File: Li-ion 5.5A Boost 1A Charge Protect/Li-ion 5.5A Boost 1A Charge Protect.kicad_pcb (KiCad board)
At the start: 2 copper layers, 51.5 x 32 mm, 58 parts, among them J1 USB_C_FEMALE, Q1 BUK6D30-40E, SW1 SW_DPST, U1 AP9101CK6, U2 ECH8695R-TL-W, U3 MCP73833T, U4 PAM2423AECADJR

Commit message: Fixed position on diode.
Fixed position on diode.
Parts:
- moved D1 1.20 mm to (133.0, 86.0)

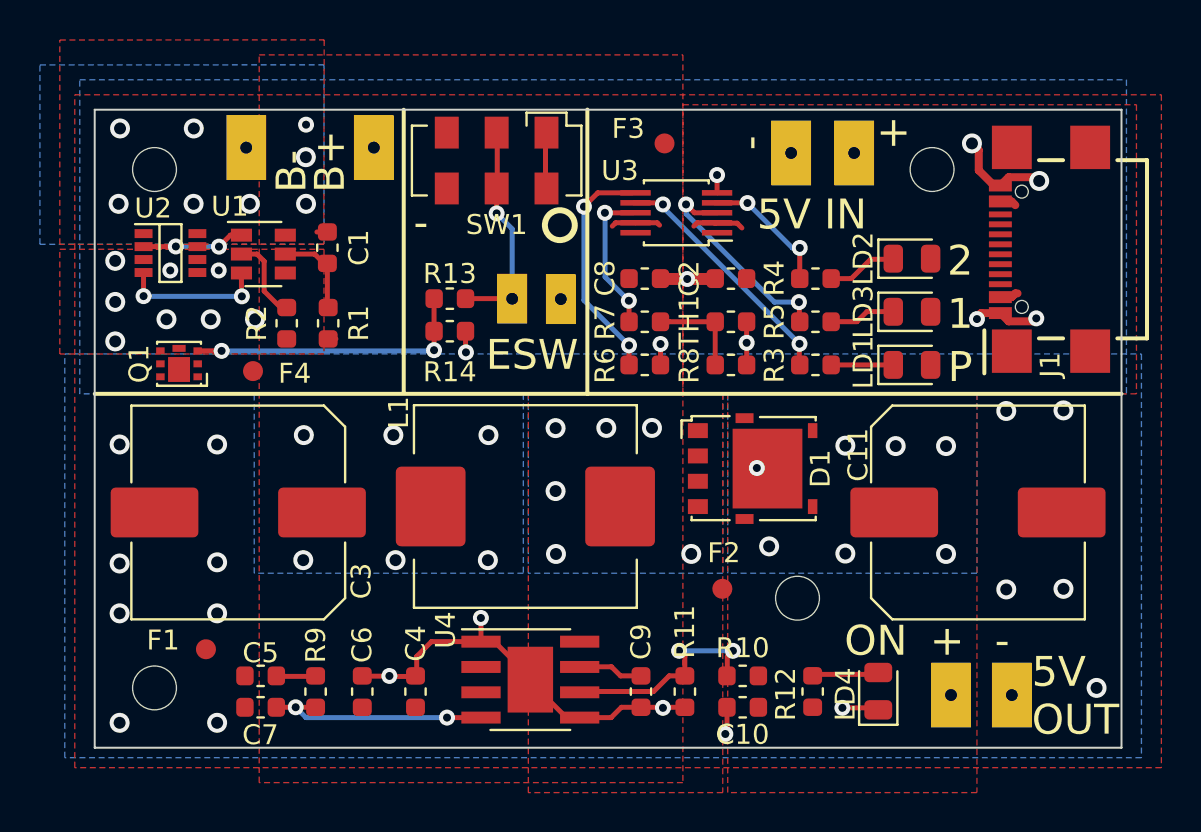
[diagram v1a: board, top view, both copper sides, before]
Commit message: Updates for footprint corrections.
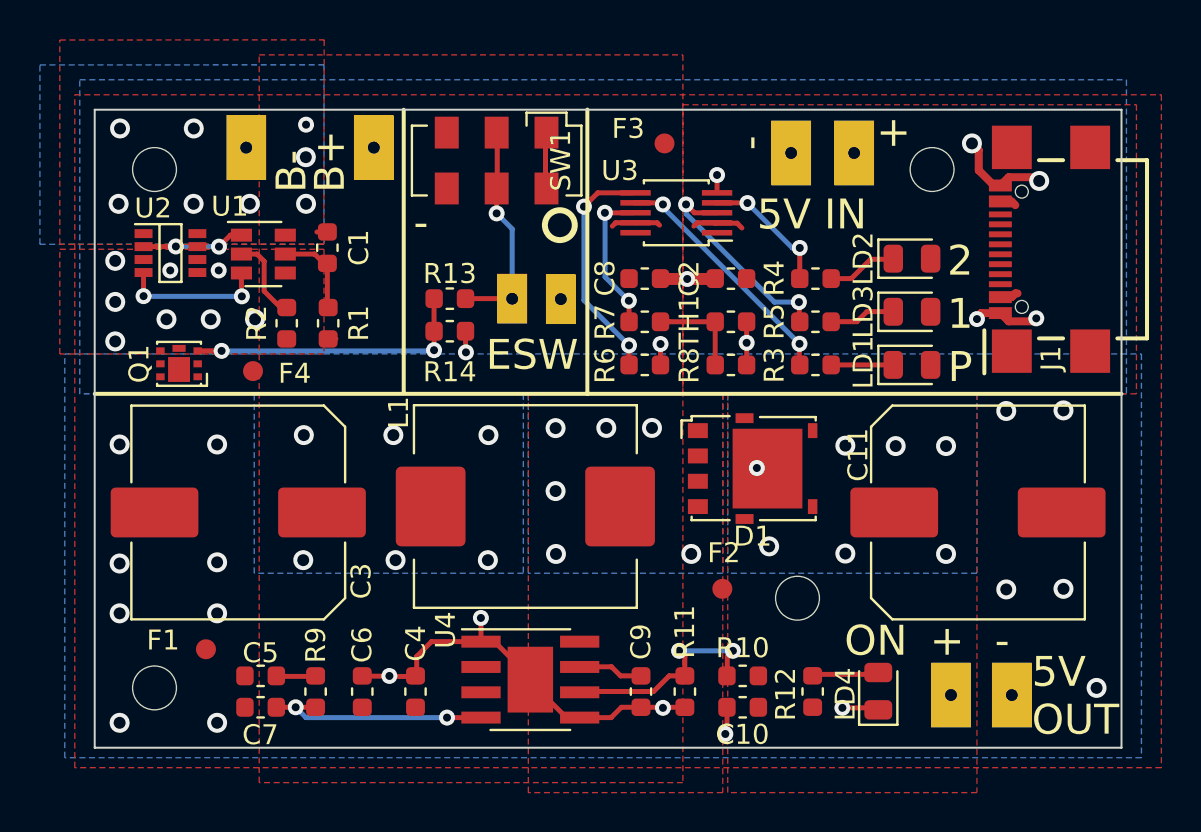
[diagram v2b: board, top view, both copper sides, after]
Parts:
- moved J1 2.44 mm to (148.9, 75.0)
- turned D1 to 0 degrees
- turned SW1 to 270 degrees
